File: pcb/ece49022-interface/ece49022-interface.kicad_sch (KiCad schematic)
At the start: 0 parts

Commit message: Interface
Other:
- added sheet RP Pico 2 W (RP2350_60QFN_minimal.kicad_sch)
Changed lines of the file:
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@@
 	(generator_version "9.0")
 	(paper "A4")
+	(sheet
+		(at 52.07 46.99)
+		(size 24.13 30.48)
+		(exclude_from_sim no)
+		(in_bom yes)
+		(on_board yes)
+		(dnp no)
+		(fields_autoplaced yes)
+		(stroke
+			(width 0.1524)
+			(type solid)
+		)
+		(fill
+			(color 0 0 0 0.0000)
+		)
+		(property "Sheetname" "RP Pico 2 W"
+			(at 52.07 46.2784 0)
+			(effects
+				(font
+					(size 1.27 1.27)
+				)
+				(justify left bottom)
+			)
+		)
+		(property "Sheetfile" "RP2350_60QFN_minimal.kicad_sch"
+			(at 52.07 78.0546 0)
+			(effects
+				(font
+					(size 1.27 1.27)
+				)
+				(justify left top)
+			)
+		)
+		(instances
+			(project "ece49022-interface"
+				(path "/ad062fbe-cbe6-4ffd-876d-97a59a1c7176"
+					(page "2")
+				)
+			)
+		)
+	)
 	(sheet_instances
 		(path "/"

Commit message: Interface
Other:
- added sheet Buzzer Driver (buzzerdriver.kicad_sch)
- added sheet LED Driver (leddriver.kicad_sch)
- added sheet Lock Actuation (lockactuator.kicad_sch)
- added sheet Power (interfacepower.kicad_sch)

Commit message: interface
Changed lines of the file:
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@@
 	(wire
 		(pts
-			(xy 91.44 114.3) (xy 91.44 105.41)
-		)
-		(stroke
-			(width 0)
-			(type default)
-		)
-	)
-	(wire
-		(pts
-			(xy 54.61 109.22) (xy 46.99 109.22)
-		)
-		(stroke
-			(width 0)
-			(type default)
-		)
-	)
-	(wire
-		(pts
-			(xy 81.28 109.22) (xy 81.28 105.41)
-		)
-		(stroke
-			(width 0)
-			(type default)
-		)
-	)
-	(wire
-		(pts
-			(xy 73.66 114.3) (xy 91.44 114.3)
-		)
-		(stroke
-			(width 0)
-			(type default)
-		)
-	)
-	(wire
-		(pts
-			(xy 73.66 109.22) (xy 81.28 109.22)
-		)
-		(stroke
-			(width 0)
-			(type default)
-		)
-	)
-	(wire
-		(pts
-			(xy 73.66 119.38) (xy 91.44 119.38)
-		)
-		(stroke
-			(width 0)
-			(type default)
-		)
-	)
-	(wire
-		(pts
-			(xy 91.44 119.38) (xy 91.44 125.73)
-		)
-		(stroke
-			(width 0)
-			(type default)
-		)
-	)
-	(wire
-		(pts
-			(xy 46.99 109.22) (xy 46.99 104.14)
+			(xy 80.01 53.34) (xy 80.01 44.45)
+		)
+		(stroke
+			(width 0)
+			(type default)
+		)
+	)
+	(wire
+		(pts
+			(xy 43.18 48.26) (xy 35.56 48.26)
+		)
+		(stroke
+			(width 0)
+			(type default)
+		)
+	)
+	(wire
+		(pts
+			(xy 69.85 48.26) (xy 69.85 44.45)
+		)
+		(stroke
+			(width 0)
+			(type default)
+		)
+	)
+	(wire
+		(pts
+			(xy 62.23 53.34) (xy 80.01 53.34)
+		)
+		(stroke
+			(width 0)
+			(type default)
+		)
+	)
+	(wire
+		(pts
+			(xy 62.23 48.26) (xy 69.85 48.26)
+		)
+		(stroke
+			(width 0)
+			(type default)
+		)
+	)
+	(wire
+		(pts
+			(xy 62.23 58.42) (xy 80.01 58.42)
+		)
+		(stroke
+			(width 0)
+			(type default)
+		)
+	)
+	(wire
+		(pts
+			(xy 80.01 58.42) (xy 80.01 64.77)
+		)
+		(stroke
+			(width 0)
+			(type default)
+		)
+	)
+	(wire
+		(pts
+			(xy 35.56 48.26) (xy 35.56 43.18)
 		)
 		(stroke
@@
 	(symbol
 		(lib_id "power:GND")
-		(at 91.44 125.73 0)
+		(at 80.01 64.77 0)
 		(unit 1)
 		(exclude_from_sim no)
@@
 		(fields_autoplaced yes)
 		(property "Reference" "#PWR048"
-			(at 91.44 132.08 0)
+			(at 80.01 71.12 0)
 			(effects
 				(font
@@
 		)
 		(property "Value" "GND"
-			(at 91.44 130.81 0)
+			(at 80.01 69.85 0)
 			(effects
 				(font
@@
 		)
 		(property "Footprint" ""
-			(at 91.44 125.73 0)
+			(at 80.01 64.77 0)
 			(effects
 				(font
@@
 		)
 		(property "Datasheet" ""
-			(at 91.44 125.73 0)
+			(at 80.01 64.77 0)
 			(effects
 				(font
@@
 		)
 		(property "Description" "Power symbol creates a global label with name \"GND\" , ground"
-			(at 91.44 125.73 0)
+			(at 80.01 64.77 0)
 			(effects
 				(font
@@
 	(symbol
 		(lib_id "power:+3V3")
-		(at 81.28 105.41 0)
+		(at 69.85 44.45 0)
 		(unit 1)
 		(exclude_from_sim no)
@@
 		(fields_autoplaced yes)
 		(property "Reference" "#PWR045"
-			(at 81.28 109.22 0)
+			(at 69.85 48.26 0)
 			(effects
 				(font
@@
 		)
 		(property "Value" "+3V3"
-			(at 81.28 100.33 0)
+			(at 69.85 39.37 0)
 			(effects
 				(font
@@
 		)
 		(property "Footprint" ""
-			(at 81.28 105.41 0)
+			(at 69.85 44.45 0)
 			(effects
 				(font
@@
 		)
 		(property "Datasheet" ""
-			(at 81.28 105.41 0)
+			(at 69.85 44.45 0)
 			(effects
 				(font
@@
 		)
 		(property "Description" "Power symbol creates a global label with name \"+3V3\""
-			(at 81.28 105.41 0)
+			(at 69.85 44.45 0)
 			(effects
 				(font
@@
 	(symbol
 		(lib_id "power:+3V3")
-		(at 91.44 105.41 0)
+		(at 80.01 44.45 0)
 		(unit 1)
 		(exclude_from_sim no)
@@
 		(fields_autoplaced yes)
 		(property "Reference" "#PWR047"
-			(at 91.44 109.22 0)
+			(at 80.01 48.26 0)
 			(effects
 				(font
@@
 		)
 		(property "Value" "+5V"
-			(at 91.44 100.33 0)
+			(at 80.01 39.37 0)
 			(effects
 				(font
@@
 		)
 		(property "Footprint" ""
-			(at 91.44 105.41 0)
+			(at 80.01 44.45 0)
 			(effects
 				(font
@@
 		)
 		(property "Datasheet" ""
-			(at 91.44 105.41 0)
+			(at 80.01 44.45 0)
 			(effects
 				(font
@@
 		)
 		(property "Description" "Power symbol creates a global label with name \"+3V3\""
-			(at 91.44 105.41 0)
+			(at 80.01 44.45 0)
 			(effects
 				(font
@@
 	(symbol
 		(lib_id "power:+3V3")
-		(at 46.99 104.14 0)
+		(at 35.56 43.18 0)
 		(unit 1)
 		(exclude_from_sim no)
@@
 		(fields_autoplaced yes)
 		(property "Reference" "#PWR046"
-			(at 46.99 107.95 0)
+			(at 35.56 46.99 0)
 			(effects
 				(font
@@
 		)
 		(property "Value" "+12V"
-			(at 46.99 99.06 0)
+			(at 35.56 38.1 0)
 			(effects
 				(font
@@
 		)
 		(property "Footprint" ""
-			(at 46.99 104.14 0)
+			(at 35.56 43.18 0)
 			(effects
 				(font
@@
 		)
 		(property "Datasheet" ""
-			(at 46.99 104.14 0)
+			(at 35.56 43.18 0)
 			(effects
 				(font
@@
 		)
 		(property "Description" "Power symbol creates a global label with name \"+3V3\""
-			(at 46.99 104.14 0)
+			(at 35.56 43.18 0)
 			(effects
 				(font
@@
 	)
 	(sheet
-		(at 54.61 104.14)
+		(at 43.18 43.18)
 		(size 19.05 19.05)
 		(exclude_from_sim no)
@@
 		)
 		(property "Sheetname" "Power"
-			(at 54.61 103.4284 0)
+			(at 43.18 42.4684 0)
 			(effects
 				(font
@@
 		)
 		(property "Sheetfile" "interfacepower.kicad_sch"
-			(at 54.61 123.7746 0)
+			(at 43.18 62.8146 0)
 			(effects
 				(font
@@
 		)
 		(pin "GND" input
-			(at 73.66 119.38 0)
+			(at 62.23 58.42 0)
 			(effects
 				(font
@@
 		)
 		(pin "5V" input
-			(at 73.66 114.3 0)
+			(at 62.23 53.34 0)
 			(effects
 				(font
@@
 		)
 		(pin "12V" input
-			(at 54.61 109.22 180)
+			(at 43.18 48.26 180)
 			(effects
 				(font
@@
 		)
 		(pin "3.3V" input
-			(at 73.66 109.22 0)
+			(at 62.23 48.26 0)
 			(effects
 				(font
@@
 	)
 	(sheet
-		(at 189.23 78.74)
+		(at 44.45 95.25)
 		(size 26.67 31.75)
 		(exclude_from_sim no)
@@
 		)
 		(property "Sheetname" "Lock Actuation"
-			(at 189.23 78.0284 0)
+			(at 44.45 94.5384 0)
 			(effects
 				(font
@@
 		)
 		(property "Sheetfile" "lockactuator.kicad_sch"
-			(at 189.23 111.0746 0)
+			(at 44.45 127.5846 0)
 			(effects
 				(font
@@
 	)
 	(sheet
-		(at 52.07 46.99)
+		(at 139.7 55.88)
 		(size 24.13 30.48)
 		(exclude_from_sim no)
@@
 		)
 		(property "Sheetname" "RP Pico 2 W"
-			(at 52.07 46.2784 0)
+			(at 139.7 55.1684 0)
 			(effects
 				(font
@@
 		)
 		(property "Sheetfile" "RP2350_60QFN_minimal.kicad_sch"
-			(at 52.07 78.0546 0)
+			(at 139.7 86.9446 0)
 			(effects
 				(font
@@
 	)
 	(sheet
-		(at 137.16 106.68)
+		(at 78.74 158.75)
 		(size 22.86 29.21)
 		(exclude_from_sim no)
@@
 		)
 		(property "Sheetname" "Buzzer Driver"
-			(at 137.16 105.9684 0)
+			(at 78.74 158.0384 0)
 			(effects
 				(font
@@
 		)
 		(property "Sheetfile" "buzzerdriver.kicad_sch"
-			(at 137.16 136.4746 0)
+			(at 78.74 188.5446 0)
 			(effects
 				(font
@@
 	)
 	(sheet
-		(at 137.16 64.77)
+		(at 45.72 143.51)
 		(size 19.05 26.67)
 		(exclude_from_sim no)
@@
 		)
 		(property "Sheetname" "LED Driver"
-			(at 137.16 64.0584 0)
+			(at 45.72 142.7984 0)
 			(effects
 				(font
@@
 		)
 		(property "Sheetfile" "leddriver.kicad_sch"
-			(at 137.16 92.0246 0)
-			(effects
-				(font
+			(at 45.72 170.7646 0)
+			(effects
+				(font

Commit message: Interface update
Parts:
- added A1: RaspberryPi_Pico_W, Module:RaspberryPi_Pico_W_SMD_HandSolder, symbol MCU_Module:RaspberryPi_Pico_W
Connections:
- net GND: now also A1.13 (GND), A1.18 (GND), A1.23 (GND), A1.28 (GND), A1.3 (GND), A1.38 (GND), A1.8 (GND)
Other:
- removed sheet RP Pico 2 W
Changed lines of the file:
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@@
+		)
+	)
+	(wire
+		(pts
+			(xy 163.83 116.84) (xy 163.83 124.46)
+		)
+		(stroke
+			(width 0)
+			(type default)
 		)
 	)
@@
 	)
 	(symbol
+		(lib_id "power:GND")
+		(at 163.83 124.46 0)
+		(unit 1)
+		(exclude_from_sim no)
+		(in_bom yes)
+		(on_board yes)
+		(dnp no)
+		(fields_autoplaced yes)
+		(property "Reference" "#PWR01"
+			(at 163.83 130.81 0)
+			(effects
+				(font
+					(size 1.27 1.27)
+				)
+				(hide yes)
+			)
+		)
+		(property "Value" "GND"
+			(at 163.83 129.54 0)
+			(effects
+				(font
+					(size 1.27 1.27)
+				)
+			)
+		)
+		(property "Footprint" ""
+			(at 163.83 124.46 0)
+			(effects
+				(font
+					(size 1.27 1.27)
+				)
+				(hide yes)
+			)
+		)
+		(property "Datasheet" ""
+			(at 163.83 124.46 0)
+			(effects
+				(font
+					(size 1.27 1.27)
+				)
+				(hide yes)
+			)
+		)
+		(property "Description" "Power symbol creates a global label with name \"GND\" , ground"
+			(at 163.83 124.46 0)
+			(effects
+				(font
+					(size 1.27 1.27)
+				)
+				(hide yes)
+			)
+		)
+		(pin "1"
+		)
+		(instances
+			(project ""
+				(path "/ad062fbe-cbe6-4ffd-876d-97a59a1c7176"
+					(reference "#PWR01")
+					(unit 1)
+				)
+			)
+		)
+	)
+	(symbol
+		(lib_id "MCU_Module:RaspberryPi_Pico_W")
+		(at 163.83 81.28 0)
+		(unit 1)
+		(exclude_from_sim no)
+		(in_bom yes)
+		(on_board yes)
+		(dnp no)
+		(fields_autoplaced yes)
+		(property "Reference" "A1"
+			(at 165.9733 115.57 0)
+			(effects
+				(font
+					(size 1.27 1.27)
+				)
+				(justify left)
+			)
+		)
+		(property "Value" "RaspberryPi_Pico_W"
+			(at 165.9733 118.11 0)
+			(effects
+				(font
+					(size 1.27 1.27)
+				)
+				(justify left)
+			)
+		)
+		(property "Footprint" "Module:RaspberryPi_Pico_W_SMD_HandSolder"
+			(at 163.83 128.27 0)
+			(effects
+				(font
+					(size 1.27 1.27)
+				)
+				(hide yes)
+			)
+		)
+		(property "Datasheet" "https://datasheets.raspberrypi.com/picow/pico-w-datasheet.pdf"
+			(at 163.83 130.81 0)
+			(effects
+				(font
+					(size 1.27 1.27)
+				)
+				(hide yes)
+			)
+		)
+		(property "Description" "Versatile and inexpensive wireless microcontroller module powered by RP2040 dual-core Arm Cortex-M0+ processor up to 133 MHz, 264kB SRAM, 2MB QSPI flash, Infineon CYW43439 2.4GHz 802.11n wireless LAN; also supports Raspberry Pi Pico 2 W"
+			(at 163.83 133.35 0)
+			(effects
+				(font
+					(size 1.27 1.27)
+				)
+				(hide yes)
+			)
+		)
+		(pin "39"
+		)
+		(pin "23"
+		)
+		(pin "7"
+		)
+		(pin "15"
+		)
+		(pin "11"
+		)
+		(pin "12"
+		)
+		(pin "17"
+		)
+		(pin "20"
+		)
+		(pin "14"
+		)
+		(pin "19"
+		)
+		(pin "6"
+		)
+		(pin "29"
+		)
+		(pin "1"
+		)
+		(pin "2"
+		)
+		(pin "38"
+		)
+		(pin "18"
+		)
+		(pin "40"
+		)
+		(pin "30"
+		)
+		(pin "4"
+		)
+		(pin "5"
+		)
+		(pin "9"
+		)
+		(pin "37"
+		)
+		(pin "10"
+		)
+		(pin "16"
+		)
+		(pin "13"
+		)
+		(pin "3"
+		)
+		(pin "28"
+		)
+		(pin "8"
+		)
+		(pin "21"
+		)
+		(pin "22"
+		)
+		(pin "36"
+		)
+		(pin "24"
+		)
+		(pin "25"
+		)
+		(pin "26"
+		)
+		(pin "27"
+		)
+		(pin "35"
+		)
+		(pin "31"
+		)
+		(pin "33"
+		)
+		(pin "32"
+		)
+		(pin "34"
+		)
+		(instances
+			(project ""
+				(path "/ad062fbe-cbe6-4ffd-876d-97a59a1c7176"
+					(reference "A1")
+					(unit 1)
+				)
+			)
+		)
+	)
+	(symbol
 		(lib_id "power:+3V3")
 		(at 35.56 43.18 0)
@@
 				)
 			)
-		)
-	)
-	(sheet
-		(at 139.7 55.88)
-		(size 24.13 30.48)
-		(exclude_from_sim no)
-		(in_bom yes)
-		(on_board yes)
-		(dnp no)
-		(fields_autoplaced yes)
-		(stroke
-			(width 0.1524)
-			(type solid)
-		)
-		(fill
-			(color 0 0 0 0.0000)
-		)
-		(property "Sheetname" "RP Pico 2 W"
-			(at 139.7 55.1684 0)
-			(effects
-				(font
-					(size 1.27 1.27)
-				)
-				(justify left bottom)
-			)
-		)
-		(property "Sheetfile" "RP2350_60QFN_minimal.kicad_sch"
-			(at 139.7 86.9446 0)
-			(effects
-				(font
-					(size 1.27 1.27)
-				)
-				(justify left top)
-			)
-		)
-		(instances
-			(project "ece49022-interface"
-				(path "/ad062fbe-cbe6-4ffd-876d-97a59a1c7176"
-					(page "2")
-				)
-			)

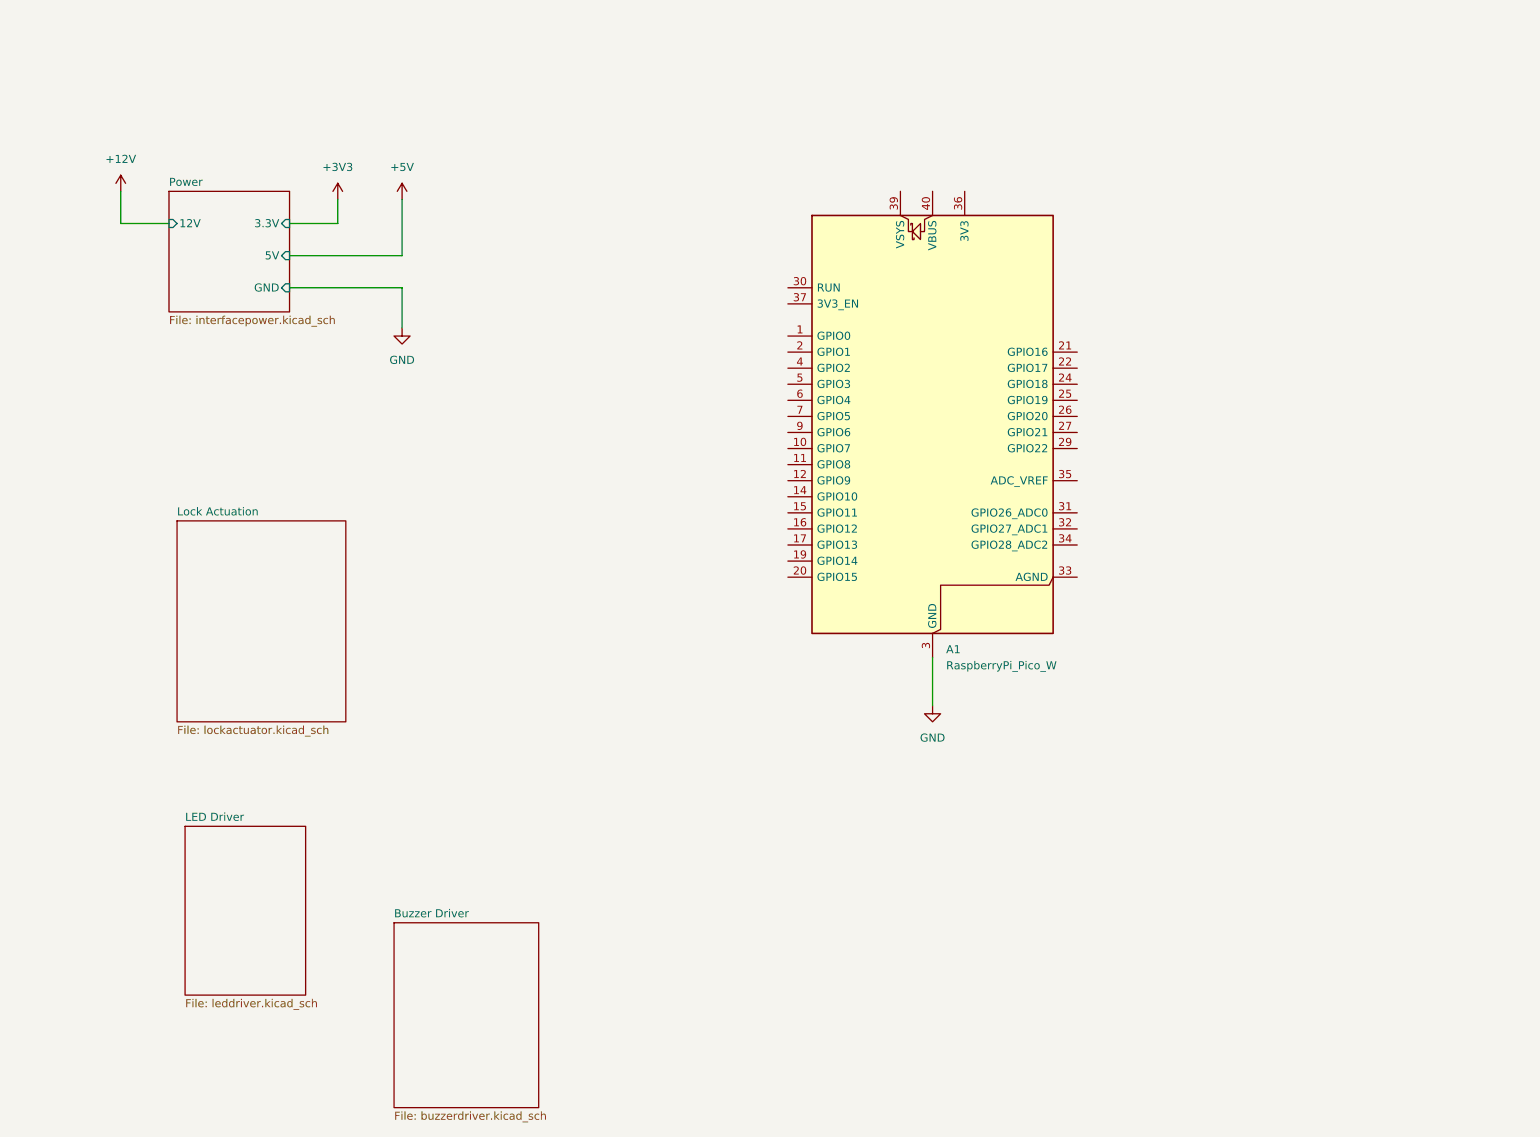
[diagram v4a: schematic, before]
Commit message: edited shelf power and added power for interface PCB
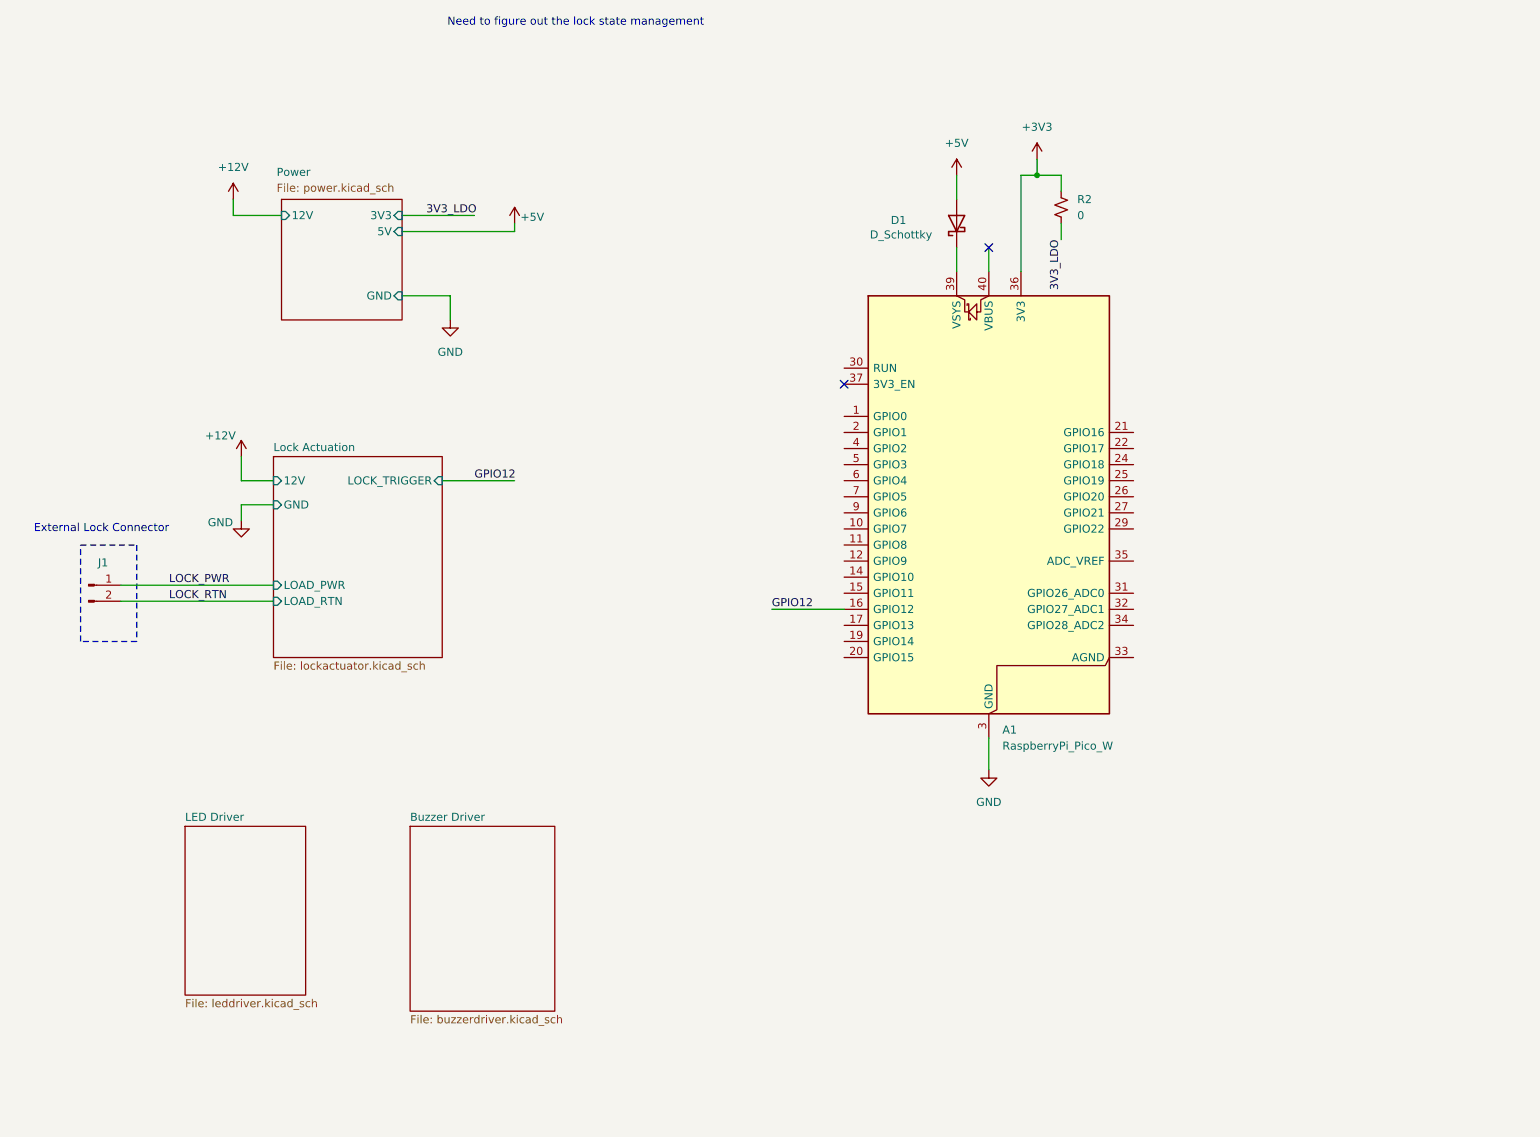
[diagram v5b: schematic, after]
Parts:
- added D1: D_Schottky, symbol Device:D_Schottky
- added J1: Conn_01x02_Pin, symbol Connector:Conn_01x02_Pin
- added R2: 0, symbol Device:R_Small_US
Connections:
- net +3V3: now also A1.36 (3V3), R2.1
- net +5V: now also D1.2 (A)
- net GPIO12: now reaches A1.16 (GPIO12)
- net at A1.39 (VSYS): now also D1.1 (K)
- new net 3V3_LDO: R2.2
- new net LOCK_PWR: J1.1 (Pin_1)
- new net LOCK_RTN: J1.2 (Pin_2)
- no-connect marks 0 -> 2
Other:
- sheet Lock Actuation ports: added 12V, GND, LOAD_PWR, LOAD_RTN, LOCK_TRIGGER; removed none
- sheet Power: file interfacepower.kicad_sch -> power.kicad_sch
- sheet Power ports: added 3V3; removed 3.3V
- note added: "External Lock Connector"
- note added: "Need to figure out the lock state management"
- moved on the sheet: A1

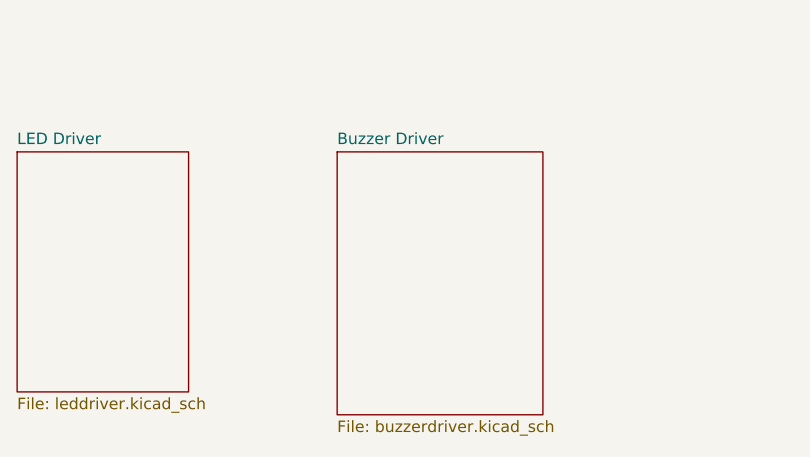
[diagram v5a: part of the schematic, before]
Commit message: Buzzer
Updated buzzer schematic
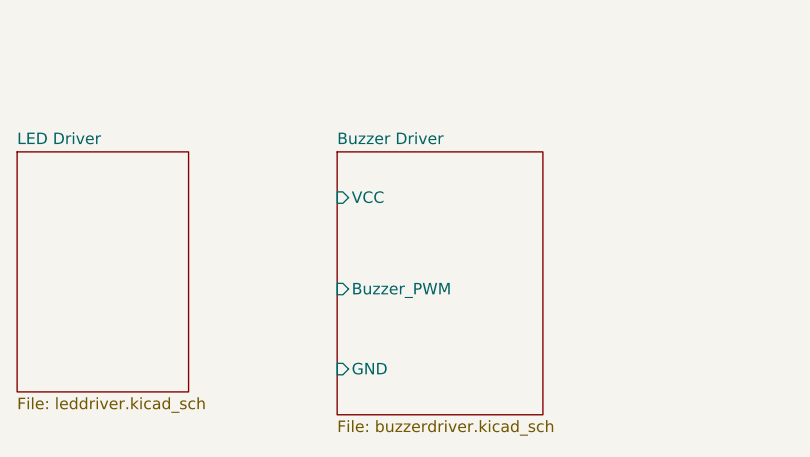
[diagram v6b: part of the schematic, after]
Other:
- sheet Buzzer Driver ports: added Buzzer_PWM, GND, VCC; removed none
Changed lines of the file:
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@@
+			)
+		)
+		(pin "Buzzer_PWM" input
+			(at 81.28 158.75 180)
+			(effects
+				(font
+					(size 1.27 1.27)
+				)
+				(justify left)
+			)
+		)
+		(pin "GND" input
+			(at 81.28 167.64 180)
+			(effects
+				(font
+					(size 1.27 1.27)
+				)
+				(justify left)
+			)
+		)
+		(pin "VCC" input
+			(at 81.28 148.59 180)
+			(effects
+				(font
+					(size 1.27 1.27)
+				)
+				(justify left)
 			)
 		)

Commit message: Interface
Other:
- sheet LED Driver ports: added GND, PWM_B, PWM_G, PWM_R; removed none
- moved on the sheet: A1, D1, J1, R2

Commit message: Update ece49022-interface.kicad_sch
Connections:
- net 3V3_LDO is gone; now on net +3V3: R2.2
- net GPIO7: now reaches A1.10 (GPIO7)
- net GPIO8: now reaches A1.11 (GPIO8)
- net GPIO16: now reaches A1.21 (GPIO16)
- net GPIO6: now reaches A1.9 (GPIO6)
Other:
- note added: "Barcode Scanner"
